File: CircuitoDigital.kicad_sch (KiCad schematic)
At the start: 10 parts, among them J7 Conn_01x02, J8 Conn_01x02, J9 Conn_02x09_Odd_Even, U1 LM7805, U2 ESP32-DEVKIT-V1

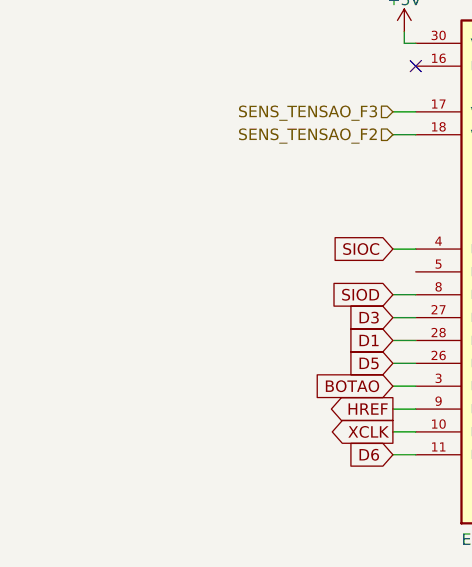
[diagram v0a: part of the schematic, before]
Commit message: Adicionado trimpots para a regulagem da entrada dos sensores de tensão. Adicionou-se também um capacitor de desacolpamento para o ESP32.
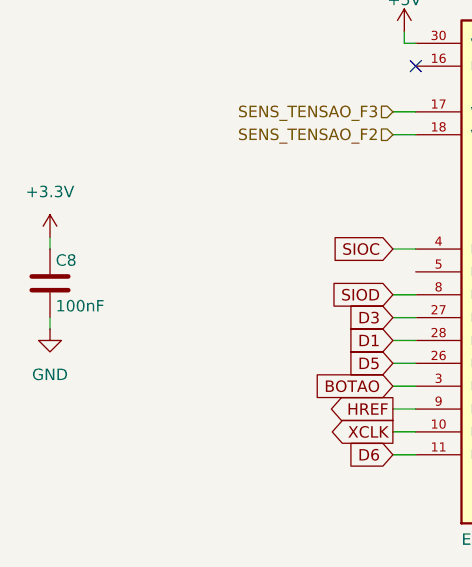
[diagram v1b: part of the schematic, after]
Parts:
- added C8: 100nF, Capacitor_THT:C_Rect_L7.0mm_W2.0mm_P5.00mm, symbol Device:C
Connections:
- net +3V3: now also C8.1
- net GND: now also C8.2
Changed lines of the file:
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@@
+    (stroke (width 0) (type default) (color 0 0 0 0))
+  )
+  (wire (pts (xy 58.42 119.38) (xy 58.42 120.65))
     (stroke (width 0) (type default) (color 0 0 0 0))
   )
@@
   )
   (wire (pts (xy 215.9 63.5) (xy 215.9 60.325))
+    (stroke (width 0) (type default) (color 0 0 0 0))
+  )
+  (wire (pts (xy 58.42 128.27) (xy 58.42 129.54))
     (stroke (width 0) (type default) (color 0 0 0 0))
   )
@@
     (pin "1")
   )
+  (symbol (lib_id "power:+3.3V") (at 58.42 119.38 0) (unit 1)
+    (in_bom yes) (on_board yes) (fields_autoplaced)
+    (property "Reference" "#PWR?" (id 0) (at 58.42 123.19 0)
+      (effects (font (size 1.27 1.27)) hide)
+    )
+    (property "Value" "+3.3V" (id 1) (at 58.42 114.3 0))
+    (property "Footprint" "" (id 2) (at 58.42 119.38 0)
+      (effects (font (size 1.27 1.27)) hide)
+    )
+    (property "Datasheet" "" (id 3) (at 58.42 119.38 0)
+      (effects (font (size 1.27 1.27)) hide)
+    )
+    (pin "1")
+  )
   (symbol (lib_id "power:GND") (at 130.81 149.86 0) (unit 1)
     (in_bom yes) (on_board yes)
@@
     (pin "1")
   )
+  (symbol (lib_id "Device:C") (at 58.42 124.46 0) (unit 1)
+    (in_bom yes) (on_board yes)
+    (property "Reference" "C8" (id 0) (at 59.055 121.92 0)
+      (effects (font (size 1.27 1.27)) (justify left))
+    )
+    (property "Value" "100nF" (id 1) (at 59.055 127 0)
+      (effects (font (size 1.27 1.27)) (justify left))
+    )
+    (property "Footprint" "Capacitor_THT:C_Rect_L7.0mm_W2.0mm_P5.00mm" (id 2) (at 59.3852 128.27 0)
+      (effects (font (size 1.27 1.27)) hide)
+    )
+    (property "Datasheet" "~" (id 3) (at 58.42 124.46 0)
+      (effects (font (size 1.27 1.27)) hide)
+    )
+    (pin "1")
+    (pin "2")
+  )
   (symbol (lib_id "power:+5V") (at 97.79 96.52 0) (unit 1)
     (in_bom yes) (on_board yes)
@@
     (pin "2")
   )
+  (symbol (lib_id "power:GND") (at 58.42 129.54 0) (unit 1)
+    (in_bom yes) (on_board yes) (fields_autoplaced)
+    (property "Reference" "#PWR?" (id 0) (at 58.42 135.89 0)
+      (effects (font (size 1.27 1.27)) hide)
+    )
+    (property "Value" "GND" (id 1) (at 58.42 134.62 0))
+    (property "Footprint" "" (id 2) (at 58.42 129.54 0)
+      (effects (font (size 1.27 1.27)) hide)
+    )
+    (property "Datasheet" "" (id 3) (at 58.42 129.54 0)
+      (effects (font (size 1.27 1.27)) hide)
+    )
+    (pin "1")
+  )
   (symbol (lib_id "power:GND") (at 215.9 86.995 0) (unit 1)

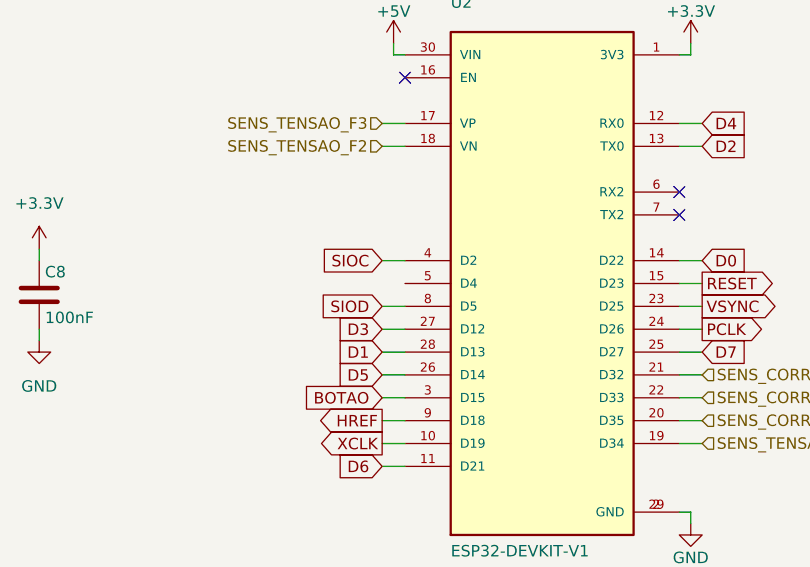
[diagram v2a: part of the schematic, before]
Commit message: Definido todos os footprints para os componentes e feito o DRC
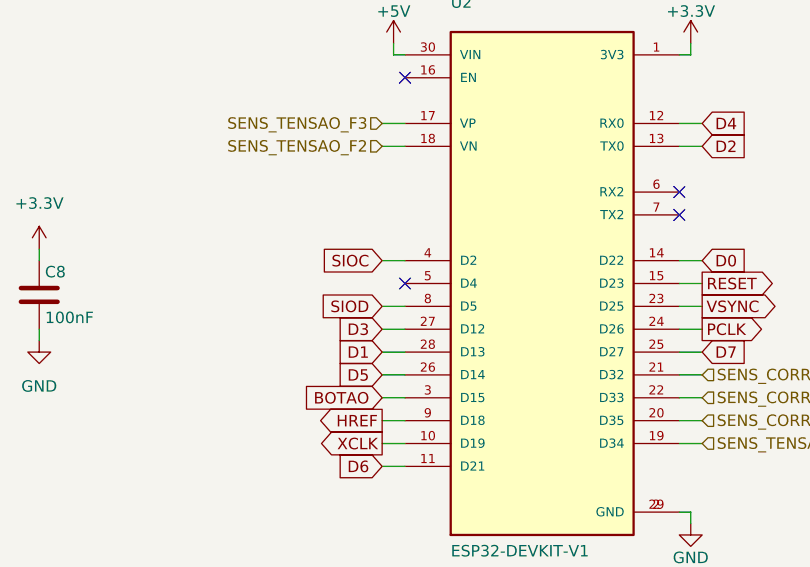
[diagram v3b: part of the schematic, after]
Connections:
- no-connect marks 4 -> 5
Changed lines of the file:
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@@
   (no_connect (at 99.06 100.33))
   (no_connect (at 129.54 115.57))
+  (no_connect (at 99.06 123.19))
   (no_connect (at 129.54 113.03))
   (no_connect (at 218.44 139.7))

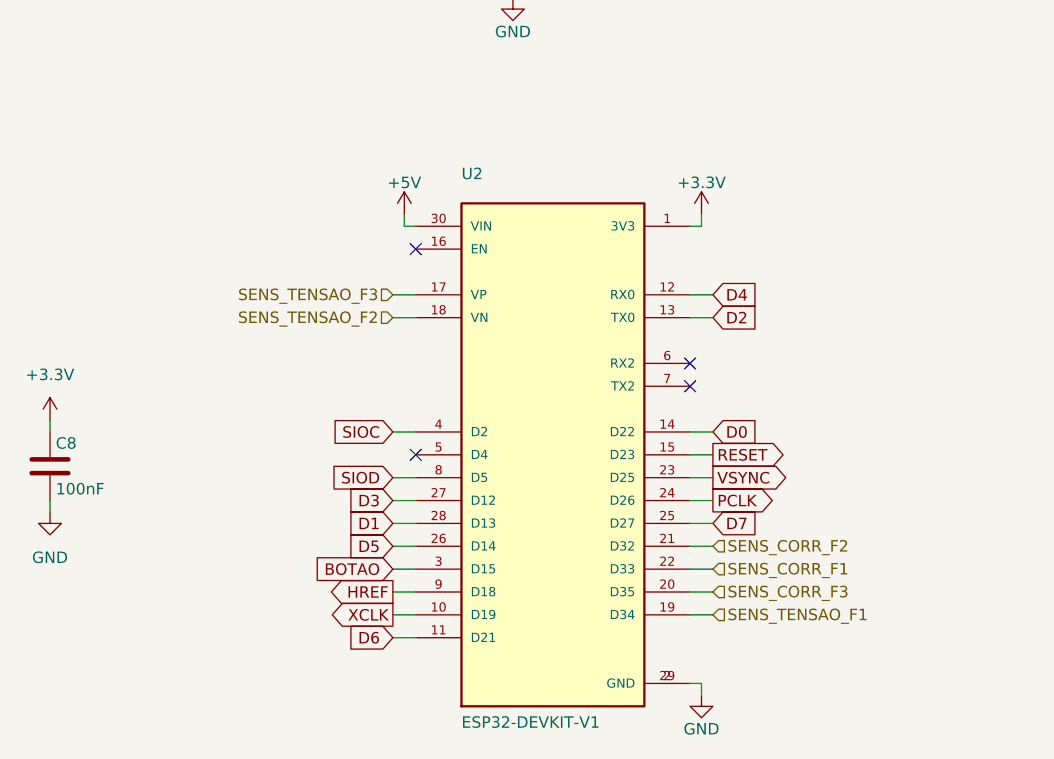
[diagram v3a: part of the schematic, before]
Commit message: PCB e modelo 3D foram completados. As alterações necessárias foram feitas no esquemático para refletir o projeto desenvolvido na PCB. Teve-se que alterar o modelo do ESP32 para aquele que foi adquirido para o projeto.
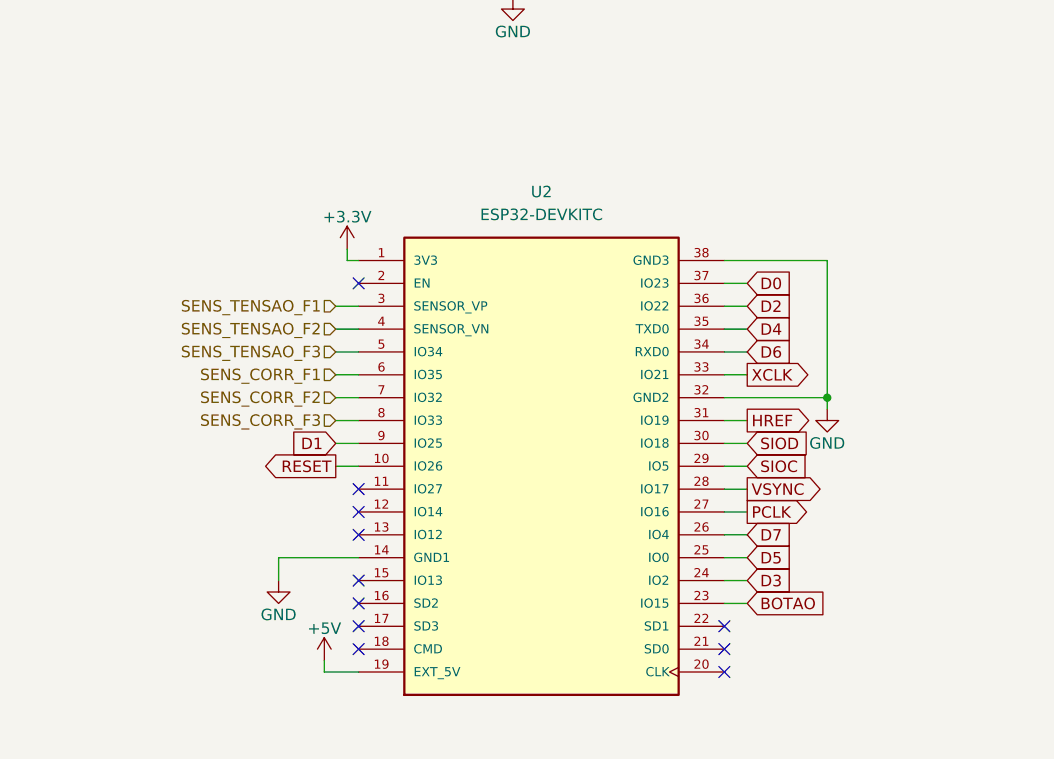
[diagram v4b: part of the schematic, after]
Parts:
- removed C8: 100nF, Capacitor_THT:C_Rect_L7.0mm_W2.0mm_P5.00mm, symbol Device:C
- removed U2: ESP32-DEVKIT-V1, ESP32-DEVKIT-V1:MODULE_ESP32_DEVKIT_V1, symbol ESP32-DEVKIT-V1:ESP32-DEVKIT-V1
- added U2: ESP32-DEVKITC, MODULE_ESP32-DEVKITC, symbol ESP32-DEVKITC:ESP32-DEVKITC
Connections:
- net +3V3: now also U2.1 (3V3)
- net +5V: now also U2.19 (EXT_5V)
- net BOTAO: now also U2.23 (IO15)
- net D0: now also U2.37 (IO23)
- net D1: now also U2.9 (IO25)
- net D2: now also U2.36 (IO22)
- net D3: now also U2.24 (IO2)
- net D4: now also U2.35 (TXD0)
- net D5: now also U2.25 (IO0)
- net D6: now also U2.34 (RXD0)
- net D7: now also U2.26 (IO4)
- net GND: now also U2.14 (GND1), U2.32 (GND2), U2.38 (GND3)
- net HREF: now also U2.31 (IO19)
- net PCLK: now also U2.27 (IO16)
- net RESET: now also U2.10 (IO26)
- net SENS_CORR_F1: now also U2.6 (IO35)
- net SENS_CORR_F2: now also U2.7 (IO32)
- net SENS_CORR_F3: now also U2.8 (IO33)
- net SENS_TENSAO_F1: now also U2.3 (SENSOR_VP)
- net SENS_TENSAO_F2: now also U2.4 (SENSOR_VN)
- net SENS_TENSAO_F3: now also U2.5 (IO34)
- net SIOC: now also U2.29 (IO5)
- net SIOD: now also U2.30 (IO18)
- net VSYNC: now also U2.28 (IO17)
- net XCLK: now also U2.33 (IO21)
- no-connect marks 5 -> 12
